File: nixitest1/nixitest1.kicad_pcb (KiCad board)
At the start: 2 copper layers, 27 parts, among them Q1 60V 3A, Q10 HVN, Q11 HVN, Q12 HVN, Q13 HVN, Q2 HVN, Q3 HVN, Q4 HVN, Q5 HVN, Q6 HVN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

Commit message: Update design.
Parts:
- removed R5: 18kΩ 1206 1% 250mW, Resistor_SMD:R_1206_3216Metric
- added C2: 10uF 25V, Capacitor_SMD:C_0603_1608Metric, F.Cu at (94.2, 64.5)
- added C3: 100n, Capacitor_SMD:C_0402_1005Metric, F.Cu at (83.5, 69.8)
- added J1: MSYS, Connector_PinHeader_2.54mm:PinHeader_2x05_P2.54mm_Horizontal, F.Cu at (84.9, 61.6)
- added J2: ~, rawpad22:rawpad22, F.Cu at (83.0, 95.0)
- added J3: ~, rawpad22:rawpad22, F.Cu at (90.0, 95.0)
- added J4: ~, rawpad22:rawpad22, F.Cu at (97.0, 95.0)
- moved NE2 49.5 mm to (80.2, 73.5), turned to -90 degrees
- moved R6 39.9 mm to (82.5, 89.1), turned to -150 degrees
- moved C1 34.8 mm to (97.9, 67.0), turned to 180 degrees
- moved R3 33.8 mm to (85.3, 64.1)
- moved NE1 33.8 mm to (80.2, 86.3), turned to -90 degrees
- moved Q9 33.5 mm to (93.0, 77.0), turned to 90 degrees
- moved R7 32.4 mm to (81.5, 82.5), turned to 180 degrees
- moved Q2 29.4 mm to (86.0, 77.7), turned to 180 degrees
- moved T1 22.9 mm to (94.0, 67.4), turned to -90 degrees
- moved Q1 21.9 mm to (90.4, 67.5)
- moved Q13 19.4 mm to (81.4, 79.0), turned to -90 degrees
- moved R1 18.9 mm to (90.2, 64.7)
- moved R2 17.7 mm to (92.0, 74.0)
- moved Q5 17.1 mm to (98.1, 82.0), turned to 180 degrees
- moved R4 9.02 mm to (98.0, 72.4), turned to 180 degrees
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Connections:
- NE1 pad 1: Net-(NE1-Pad1) -> ANODE
- NE2 pad 1: Net-(NE1-Pad1) -> ANODE
- U1 pad 15: unconnected-(U1-Pad15) -> PGM
- U1 pad 19: unconnected-(U1-Pad19) -> URX
- U1 pad 20: unconnected-(U1-Pad20) -> UTX
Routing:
- net GND: track 0.00 -> 140.2 mm, vias 0 -> 60
- net ANODE: track 0.00 -> 33.2 mm, vias 0 -> 2
- net +5V: track 0.00 -> 31.3 mm, vias 0 -> 1
- net DIG_5: track 0.00 -> 29.3 mm, vias 0 -> 2
- net DIG_4: track 0.00 -> 26.9 mm, vias 0 -> 2
- net DIG_3: track 0.00 -> 26.2 mm, vias 0 -> 2
- net DIG_8: track 0.00 -> 24.3 mm, vias 0 -> 2
- net DIG_7: track 0.00 -> 23.4 mm, vias 0 -> 2
- net DIG_2: track 0.00 -> 22.9 mm, vias 0 -> 2
- net DIG_6: track 0.00 -> 21.8 mm, vias 0 -> 2
- net DIG_9: track 0.00 -> 19.4 mm, vias 0 -> 2
- net DIG_1: track 0.00 -> 18.5 mm, vias 0 -> 2
- net Net-(C1-Pad1): track 0.00 -> 18.3 mm
- net HVVMON: track 0.00 -> 15.6 mm, vias 0 -> 2
- net DIG_0: track 0.00 -> 14.6 mm, vias 0 -> 2
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- added copper zone on B.Cu, net GND
- added copper zone on F.Cu, net GND
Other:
- board outline added: 22 x 38 mm
- board text added: "*"
- board text added: "nixitest1 rev-"

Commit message: Ok actually ready for production.
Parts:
- R1: value 300mΩ -> 500mΩ; footprint Resistor_SMD:R_1206_3216Metric -> Resistor_SMD:R_0805_2012Metric
- moved C2 0.55 mm to (94.0, 64.9)
- moved J1 0.37 mm to (84.9, 62.0)
- moved T1 0.26 mm to (94.0, 67.7)
- moved R1 0.23 mm to (90.3, 64.9)
- moved R3 0.23 mm to (85.3, 64.3)
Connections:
- J3 pad 1: GND -> +5V
- J4 pad 1: GND -> PGM
- U1 pad 1: HVCTL -> DIG_AUX
- U1 pad 2: DIG_AUX -> HVCTL
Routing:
- net +5V: track 31.3 -> 78.6 mm, vias 1 -> 2
- net PGM: track 11.1 -> 55.9 mm, vias 0 -> 1
- net GND: track 140.2 -> 172.8 mm, vias 60 -> 65
- net DIG_AUX: track 13.3 -> 14.1 mm
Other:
- board text added: "GND"
- board text added: "PGM"
- board text added: "VCC"

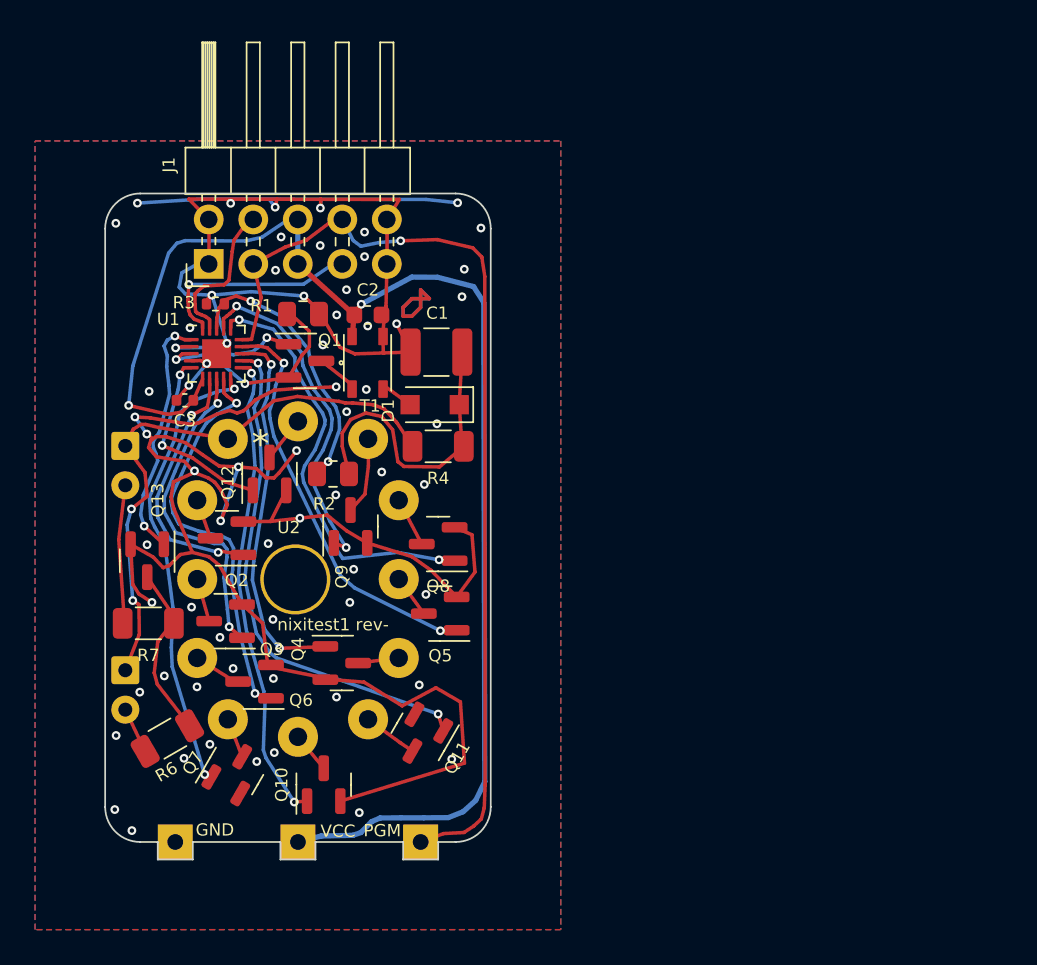
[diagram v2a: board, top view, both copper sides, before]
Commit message: Update design based on tests of first rev.
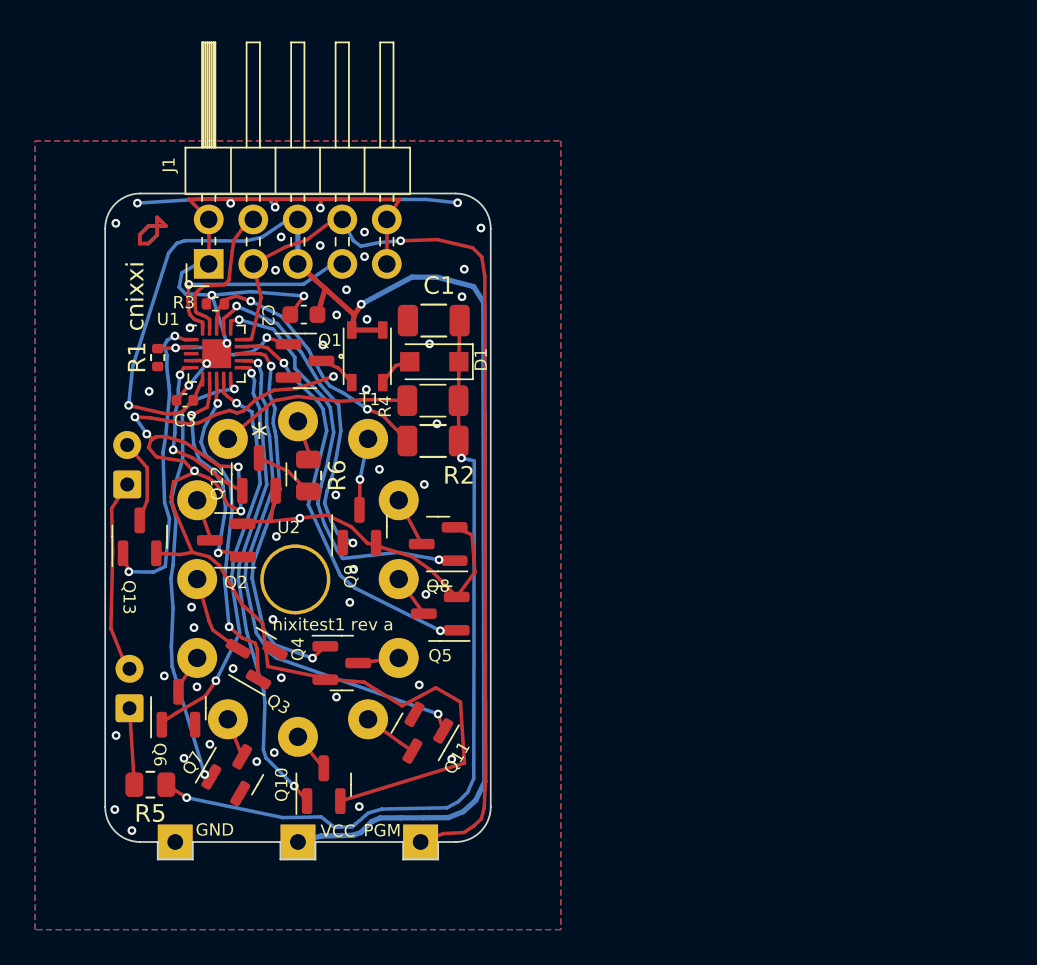
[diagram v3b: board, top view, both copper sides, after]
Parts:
- removed R7: 18kΩ 1206 1% 250mW, Resistor_SMD:R_1206_3216Metric
- added R5: 68kΩ 125mW, Resistor_SMD:R_0805_2012Metric, F.Cu at (81.6, 91.7)
- C1: footprint Capacitor_SMD:C_1210_3225Metric -> Capacitor_SMD:C_1206_3216Metric
- R1: value 500mΩ -> 10k; footprint Resistor_SMD:R_0805_2012Metric -> Resistor_SMD:R_0402_1005Metric
- R2: footprint Resistor_SMD:R_0805_2012Metric -> Resistor_SMD:R_1206_3216Metric
- R4: value 18kΩ 1206 1% 250mW -> 15kΩ 1206 1% 250mW
- R6: value 18kΩ 1206 1% 250mW -> 68kΩ 125mW; footprint Resistor_SMD:R_1206_3216Metric -> Resistor_SMD:R_0805_2012Metric
- moved R6 17.0 mm to (90.6, 74.1), turned to -90 degrees
- moved R1 8.65 mm to (82.0, 67.4), turned to 90 degrees
- moved R2 6.01 mm to (97.7, 72.1)
- moved Q6 4.60 mm to (83.2, 87.4), turned to 90 degrees
- moved C2 3.65 mm to (90.3, 64.9), turned to 180 degrees
- moved R4 2.62 mm to (97.7, 69.8)
- moved Q3 2.56 mm to (87.4, 84.4), turned to 150 degrees
- moved D1 2.45 mm to (97.8, 67.6)
- moved C1 1.81 mm to (97.8, 65.2)
- moved Q13 1.43 mm to (81.0, 77.6), turned to 90 degrees
- moved Q12 0.60 mm to (87.8, 74.0)
- moved Q9 0.51 mm to (93.5, 77.0)
- moved T1 0.37 mm to (94.0, 67.3)
- moved NE1 0.24 mm to (80.4, 86.3), turned to 90 degrees
- moved Q2 0.13 mm to (85.9, 77.8)
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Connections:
- net Net-(C1-Pad1) renamed HV
- NE1 pad 1: ANODE -> Net-(NE1-Pad1)
- NE1 pad 2: Net-(NE1-Pad2) -> Net-(NE2-Pad1)
- NE2 pad 1: ANODE -> Net-(NE2-Pad1)
- NE2 pad 2: Net-(NE2-Pad2) -> CATHAUX
- Q1 pad 2: HVIMON -> GND
- Q12 pad 3: CATHDOT -> Net-(Q12-Pad3)
- R1 pad 1: HVIMON -> GND
- R1 pad 2: GND -> HVCTL
- R6 pad 1: CATHAUX -> CATHDOT
- R6 pad 2: Net-(NE1-Pad2) -> Net-(Q12-Pad3)
- T1 pad 2: GND -> +5V
- U1 pad 3: HVIMON -> unconnected-(U1-Pad3)
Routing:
- net HV: track 18.3 -> 45.0 mm, vias 0 -> 2
- net GND: track 172.8 -> 147.7 mm, vias 65 -> 60
- net ANODE: track 33.1 -> 11.1 mm, vias 2 -> 0
- net HVIMON: track 12.9 -> 0.00 mm, vias 2 -> 0
- net Net-(NE2-Pad1): track 0.00 -> 11.0 mm
- net Net-(NE2-Pad2): track 7.63 -> 0.00 mm
- net CATHAUX: track 9.99 -> 4.81 mm
- net Net-(NE1-Pad1): track 0.00 -> 4.37 mm
- net DIG_AUX: track 14.1 -> 17.8 mm
- net Net-(Q12-Pad3): track 0.00 -> 3.45 mm
- net +5V: track 78.6 -> 81.6 mm
- net Net-(NE1-Pad2): track 2.64 -> 0.00 mm
- net CATH1: track 2.50 -> 4.85 mm
- net DIG_0: track 14.6 -> 12.6 mm
- net DIG_DOT: track 10.9 -> 9.81 mm
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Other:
- board text added: "cnixxi"
- board text added: "nixitest1 rev a"
- board text removed: "nixitest1 rev-"

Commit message: Update schematic and design.
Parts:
- added J5: ~, rawpad22:rawpad22, F.Cu at (94.0, 95.0)
- added J6: ~, rawpad22:rawpad22, F.Cu at (98.0, 95.0)
- moved J4 11.0 mm to (86.0, 95.0)
- moved J2 1.00 mm to (82.0, 95.0)
- moved NE2 0.22 mm to (80.4, 73.6)
- moved R4 0.09 mm to (97.7, 69.9)
- moved R2 0.06 mm to (97.7, 72.2)
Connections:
- J4 pad 1: PGM -> URX
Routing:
- net UTX: track 12.2 -> 52.8 mm, vias 1 -> 3
- net URX: track 8.86 -> 46.2 mm, vias 0 -> 1
- net GND: track 147.7 -> 131.3 mm, vias 60 -> 76
- net HV: track 45.0 -> 41.4 mm
- net PGM: track 55.9 -> 56.9 mm
- net +5V: track 81.6 -> 82.1 mm
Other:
- board size 22 x 38 mm -> 22 x 37.9 mm
- board text added: "URX"
- board text added: "UTX"

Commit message: Updte with schematic.
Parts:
- moved J2 0.38 mm to (82.0, 95.4)
- moved J3 0.38 mm to (90.0, 95.4)
- moved J4 0.38 mm to (86.0, 95.4)
- moved J5 0.38 mm to (94.0, 95.4)
- moved J6 0.38 mm to (98.0, 95.4)
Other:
- board size 22 x 37.9 mm -> 22 x 38.2 mm
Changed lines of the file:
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@@
     )
     (pad_to_mask_clearance 0)
+    (grid_origin 79 93)
     (pcbplotparams
       (layerselection 0x00010fc_ffffffff)
@@
       (drillshape 0)
       (scaleselection 1)
-      (outputdirectory "nixitest1-rev-")
+      (outputdirectory "nixitest1-revA")
     )
   )
@@
   (net 39 "unconnected-(U1-Pad3)")
   (footprint "rawpad22:rawpad22" (layer "F.Cu")
-    (at 98 95)
+    (at 98 95.375)
     (property "Sheetfile" "nixitest1.kicad_sch")
     (property "Sheetname" "")
@@
     (fp_line (start -1.6 0.8) (end -1.6 -0.8) (layer "F.Fab") (width 0.1))
     (fp_line (start -1.6 -0.8) (end 1.6 -0.8) (layer "F.Fab") (width 0.1))
-    (pad "1" smd roundrect (at -1.475 0 180) (size 1.15 1.8) (layers "F.Cu" "F.Paste" "F.Mask") (roundrect_rratio 0.217391)
+    (pad "1" smd roundrect (at -1.475 0 180) (size 1.15 1.8) (layers "F.Cu" "F.Paste" "F.Mask") (roundrect_rratio 0.2173913043)
       (net 31 "HV") (pintype "passive"))
-    (pad "2" smd roundrect (at 1.475 0 180) (size 1.15 1.8) (layers "F.Cu" "F.Paste" "F.Mask") (roundrect_rratio 0.217391)
+    (pad "2" smd roundrect (at 1.475 0 180) (size 1.15 1.8) (layers "F.Cu" "F.Paste" "F.Mask") (roundrect_rratio 0.2173913043)
       (net 1 "GND") (pintype "passive"))
     (model "${KICAD6_3DMODEL_DIR}/Capacitor_SMD.3dshapes/C_1206_3216Metric.wrl"
@@
   )
   (footprint "rawpad22:rawpad22" (layer "F.Cu")
-    (at 94 95)
+    (at 94 95.375)
     (property "Sheetfile" "nixitest1.kicad_sch")
     (property "Sheetname" "")
@@
     (fp_line (start -1 0.625) (end -1 -0.625) (layer "F.Fab") (width 0.1))
     (fp_line (start 1 -0.625) (end 1 0.625) (layer "F.Fab") (width 0.1))
-    (pad "1" smd roundrect (at -0.9125 0 270) (size 1.025 1.4) (layers "F.Cu" "F.Paste" "F.Mask") (roundrect_rratio 0.243902)
+    (pad "1" smd roundrect (at -0.9125 0 270) (size 1.025 1.4) (layers "F.Cu" "F.Paste" "F.Mask") (roundrect_rratio 0.243902439)
       (net 26 "CATHDOT") (pintype "passive"))
-    (pad "2" smd roundrect (at 0.9125 0 270) (size 1.025 1.4) (layers "F.Cu" "F.Paste" "F.Mask") (roundrect_rratio 0.243902)
+    (pad "2" smd roundrect (at 0.9125 0 270) (size 1.025 1.4) (layers "F.Cu" "F.Paste" "F.Mask") (roundrect_rratio 0.243902439)
       (net 38 "Net-(Q12-Pad3)") (pintype "passive"))
     (model "${KICAD6_3DMODEL_DIR}/Resistor_SMD.3dshapes/R_0805_2012Metric.wrl"
@@
   )
   (footprint "rawpad22:rawpad22" (layer "F.Cu")
-    (at 90 95)
+    (at 90 95.375)
     (property "Sheetfile" "nixitest1.kicad_sch")
     (property "Sheetname" "")
@@
     (fp_line (start 1.6 0.8) (end -1.6 0.8) (layer "F.Fab") (width 0.1))
     (fp_line (start 1.6 -0.8) (end 1.6 0.8) (layer "F.Fab") (width 0.1))
-    (pad "1" smd roundrect (at -1.4625 0) (size 1.125 1.75) (layers "F.Cu" "F.Paste" "F.Mask") (roundrect_rratio 0.222222)
+    (pad "1" smd roundrect (at -1.4625 0) (size 1.125 1.75) (layers "F.Cu" "F.Paste" "F.Mask") (roundrect_rratio 0.2222222222)
       (net 29 "HVVMON") (pintype "passive"))
-    (pad "2" smd roundrect (at 1.4625 0) (size 1.125 1.75) (layers "F.Cu" "F.Paste" "F.Mask") (roundrect_rratio 0.222222)
+    (pad "2" smd roundrect (at 1.4625 0) (size 1.125 1.75) (layers "F.Cu" "F.Paste" "F.Mask") (roundrect_rratio 0.2222222222)
       (net 31 "HV") (pintype "passive"))
     (model "${KICAD6_3DMODEL_DIR}/Resistor_SMD.3dshapes/R_1206_3216Metric.wrl"
@@
   )
   (footprint "rawpad22:rawpad22" (layer "F.Cu")
-    (at 86 95)
+    (at 86 95.375)
     (property "Sheetfile" "nixitest1.kicad_sch")
     (property "Sheetname" "")
@@
   )
   (footprint "rawpad22:rawpad22" (layer "F.Cu")
-    (at 82 95)
+    (at 82 95.375)
     (property "Sheetfile" "nixitest1.kicad_sch")
     (property "Sheetname" "")
@@
     (fp_line (start 1 0.625) (end -1 0.625) (layer "F.Fab") (width 0.1))
     (fp_line (start 1 -0.625) (end 1 0.625) (layer "F.Fab") (width 0.1))
-    (pad "1" smd roundrect (at -0.9125 0 180) (size 1.025 1.4) (layers "F.Cu" "F.Paste" "F.Mask") (roundrect_rratio 0.243902)
+    (pad "1" smd roundrect (at -0.9125 0 180) (size 1.025 1.4) (layers "F.Cu" "F.Paste" "F.Mask") (roundrect_rratio 0.243902439)
       (net 31 "HV") (pintype "passive"))
-    (pad "2" smd roundrect (at 0.9125 0 180) (size 1.025 1.4) (layers "F.Cu" "F.Paste" "F.Mask") (roundrect_rratio 0.243902)
+    (pad "2" smd roundrect (at 0.9125 0 180) (size 1.025 1.4) (layers "F.Cu" "F.Paste" "F.Mask") (roundrect_rratio 0.243902439)
       (net 32 "Net-(NE1-Pad1)") (pintype "passive"))
     (model "${KICAD6_3DMODEL_DIR}/Resistor_SMD.3dshapes/R_0805_2012Metric.wrl"
@@
   (gr_line (start 80.97 60.86) (end 80.97 60.36) (layer "F.Mask") (width 0.15))
   (gr_line (start 79 60) (end 79 93) (layer "Edge.Cuts") (width 0.1))
-  (gr_line (start 93.125 95.875) (end 93.125 95) (layer "Edge.Cuts") (width 0.1))
-  (gr_line (start 94.875 95.875) (end 93.125 95.875) (layer "Edge.Cuts") (width 0.1))
+  (gr_line (start 93.125 96.25) (end 93.125 95) (layer "Edge.Cuts") (width 0.1))
+  (gr_line (start 94.875 96.25) (end 93.125 96.25) (layer "Edge.Cuts") (width 0.1))
   (gr_arc (start 101 93) (mid 100.414214 94.414214) (end 99 95) (layer "Edge.Cuts") (width 0.1))
-  (gr_line (start 90.875 95.875) (end 89.125 95.875) (layer "Edge.Cuts") (width 0.1))
-  (gr_line (start 86.875 95) (end 86.875 95.875) (layer "Edge.Cuts") (width 0.1))
-  (gr_line (start 81.125 95.875) (end 82.875 95.875) (layer "Edge.Cuts") (width 0.1))
+  (gr_line (start 90.875 96.25) (end 89.125 96.25) (layer "Edge.Cuts") (width 0.1))
+  (gr_line (start 86.875 95) (end 86.875 96.25) (layer "Edge.Cuts") (width 0.1))
+  (gr_line (start 81.125 96.25) (end 82.875 96.25) (layer "Edge.Cuts") (width 0.1))
   (gr_line (start 90.875 95) (end 93.125 95) (layer "Edge.Cuts") (width 0.1))
   (gr_line (start 101 93) (end 101 60) (layer "Edge.Cuts") (width 0.1))
   (gr_arc (start 81 95) (mid 79.585786 94.414214) (end 79 93) (layer "Edge.Cuts") (width 0.1))
   (gr_line (start 82.875 95) (end 85.125 95) (layer "Edge.Cuts") (width 0.1))
-  (gr_line (start 98.875 95.875) (end 97.125 95.875) (layer "Edge.Cuts") (width 0.1))
-  (gr_line (start 82.875 95.875) (end 82.875 95) (layer "Edge.Cuts") (width 0.1))
+  (gr_line (start 98.875 96.25) (end 97.125 96.25) (layer "Edge.Cuts") (width 0.1))
+  (gr_line (start 82.875 96.25) (end 82.875 95) (layer "Edge.Cuts") (width 0.1))
   (gr_line (start 99 95) (end 98.875 95) (layer "Edge.Cuts") (width 0.1))
   (gr_line (start 81 58) (end 99 58) (layer "Edge.Cuts") (width 0.1))
   (gr_line (start 81 95) (end 81.125 95) (layer "Edge.Cuts") (width 0.1))
-  (gr_line (start 89.125 95.875) (end 89.125 95) (layer "Edge.Cuts") (width 0.1))
-  (gr_line (start 94.875 95) (end 94.875 95.875) (layer "Edge.Cuts") (width 0.1))
-  (gr_line (start 85.125 95.875) (end 85.125 95) (layer "Edge.Cuts") (width 0.1))
-  (gr_line (start 90.875 95) (end 90.875 95.875) (layer "Edge.Cuts") (width 0.1))
+  (gr_line (start 89.125 96.25) (end 89.125 95) (layer "Edge.Cuts") (width 0.1))
+  (gr_line (start 94.875 95) (end 94.875 96.25) (layer "Edge.Cuts") (width 0.1))
+  (gr_line (start 85.125 96.25) (end 85.125 95) (layer "Edge.Cuts") (width 0.1))
+  (gr_line (start 90.875 95) (end 90.875 96.25) (layer "Edge.Cuts") (width 0.1))
   (gr_arc (start 79 60) (mid 79.585786 58.585786) (end 81 58) (layer "Edge.Cuts") (width 0.1))
   (gr_line (start 86.875 95) (end 89.125 95) (layer "Edge.Cuts") (width 0.1))
-  (gr_line (start 81.125 95) (end 81.125 95.875) (layer "Edge.Cuts") (width 0.1))
+  (gr_line (start 81.125 95) (end 81.125 96.25) (layer "Edge.Cuts") (width 0.1))
   (gr_arc (start 99 58) (mid 100.414214 58.585786) (end 101 60) (layer "Edge.Cuts") (width 0.1))
-  (gr_line (start 98.875 95) (end 98.875 95.875) (layer "Edge.Cuts") (width 0.1))
-  (gr_line (start 86.875 95.875) (end 85.125 95.875) (layer "Edge.Cuts") (width 0.1))
-  (gr_line (start 97.125 95.875) (end 97.125 95) (layer "Edge.Cuts") (width 0.1))
+  (gr_line (start 98.875 95) (end 98.875 96.25) (layer "Edge.Cuts") (width 0.1))
+  (gr_line (start 86.875 96.25) (end 85.125 96.25) (layer "Edge.Cuts") (width 0.1))
+  (gr_line (start 97.125 96.25) (end 97.125 95) (layer "Edge.Cuts") (width 0.1))
   (gr_line (start 94.875 95) (end 97.125 95) (layer "Edge.Cuts") (width 0.1))
   (gr_text "*" (at 87.42 71.84 -120) (layer "B.SilkS")

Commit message: Tweak pins.
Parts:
- moved J2 0.25 mm to (82.0, 95.1)
- moved J3 0.25 mm to (90.0, 95.1)
- moved J4 0.25 mm to (86.0, 95.1)
- moved J5 0.25 mm to (94.0, 95.1)
- moved J6 0.25 mm to (98.0, 95.1)
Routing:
- net GND: vias 76 -> 79
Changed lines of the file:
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@@
   (net 39 "unconnected-(U1-Pad3)")
   (footprint "rawpad22:rawpad22" (layer "F.Cu")
-    (at 98 95.375)
+    (at 98 95.125)
     (property "Sheetfile" "nixitest1.kicad_sch")
     (property "Sheetname" "")
@@
       (effects (font (size 1 1) (thickness 0.15)))
     )
-    (pad "1" thru_hole rect (at 0 0) (size 1.75 1.75) (drill 0.9) (layers *.Cu *.Mask)
+    (pad "1" thru_hole rect (at 0 0) (size 1.75 2.25) (drill 0.9) (layers *.Cu *.Mask)
       (net 36 "UTX") (pinfunction "Pin_1") (pintype "passive"))
   )
@@
   )
   (footprint "rawpad22:rawpad22" (layer "F.Cu")
-    (at 94 95.375)
+    (at 94 95.125)
     (property "Sheetfile" "nixitest1.kicad_sch")
     (property "Sheetname" "")
@@
       (effects (font (size 1 1) (thickness 0.15)))
     )
-    (pad "1" thru_hole rect (at 0 0) (size 1.75 1.75) (drill 0.9) (layers *.Cu *.Mask)
+    (pad "1" thru_hole rect (at 0 0) (size 1.75 2.25) (drill 0.9) (layers *.Cu *.Mask)
       (net 34 "PGM") (pinfunction "Pin_1") (pintype "passive"))
   )
@@
   )
   (footprint "rawpad22:rawpad22" (layer "F.Cu")
-    (at 90 95.375)
+    (at 90 95.125)
     (property "Sheetfile" "nixitest1.kicad_sch")
     (property "Sheetname" "")
@@
       (effects (font (size 1 1) (thickness 0.15)))
     )
-    (pad "1" thru_hole rect (at 0 0) (size 1.75 1.75) (drill 0.9) (layers *.Cu *.Mask)
+    (pad "1" thru_hole rect (at 0 0) (size 1.75 2.25) (drill 0.9) (layers *.Cu *.Mask)
       (net 33 "+5V") (pinfunction "Pin_1") (pintype "passive"))
   )
@@
   )
   (footprint "rawpad22:rawpad22" (layer "F.Cu")
-    (at 86 95.375)
+    (at 86 95.125)
     (property "Sheetfile" "nixitest1.kicad_sch")
     (property "Sheetname" "")
@@
       (effects (font (size 1 1) (thickness 0.15)))
     )
-    (pad "1" thru_hole rect (at 0 0) (size 1.75 1.75) (drill 0.9) (layers *.Cu *.Mask)
+    (pad "1" thru_hole rect (at 0 0) (size 1.75 2.25) (drill 0.9) (layers *.Cu *.Mask)
       (net 35 "URX") (pinfunction "Pin_1") (pintype "passive"))
   )
   (footprint "rawpad22:rawpad22" (layer "F.Cu")
-    (at 82 95.375)
+    (at 82 95.125)
     (property "Sheetfile" "nixitest1.kicad_sch")
     (property "Sheetname" "")
@@
       (effects (font (size 1 1) (thickness 0.15)))
     )
-    (pad "1" thru_hole rect (at 0 0) (size 1.75 1.75) (drill 0.9) (layers *.Cu *.Mask)
+    (pad "1" thru_hole rect (at 0 0) (size 1.75 2.25) (drill 0.9) (layers *.Cu *.Mask)
       (net 1 "GND") (pinfunction "Pin_1") (pintype "passive"))
   )
@@
   (via (at 83.84 65.66) (size 0.5) (drill 0.25) (layers "F.Cu" "B.Cu") (free) (net 1))
   (via (at 84.07 82.77) (size 0.5) (drill 0.25) (layers "F.Cu" "B.Cu") (free) (net 1))
+  (via (at 94.625 90.125) (size 0.5) (drill 0.25) (layers "F.Cu" "B.Cu") (free) (net 1))
   (via (at 83.93 81.6) (size 0.5) (drill 0.25) (layers "F.Cu" "B.Cu") (free) (net 1))
   (via (at 87.65 90.41) (size 0.5) (drill 0.25) (layers "F.Cu" "B.Cu") (free) (net 1))
@@
   (via (at 93 92) (size 0.5) (drill 0.25) (layers "F.Cu" "B.Cu") (free) (net 1))
   (via (at 79.52 68.07) (size 0.5) (drill 0.25) (layers "F.Cu" "B.Cu") (free) (net 1))
+  (via (at 90.625 91.375) (size 0.5) (drill 0.25) (layers "F.Cu" "B.Cu") (free) (net 1))
+  (via (at 91.5 92.625) (size 0.5) (drill 0.25) (layers "F.Cu" "B.Cu") (free) (net 1))
   (via (at 99.48 83.83) (size 0.5) (drill 0.25) (layers "F.Cu" "B.Cu") (free) (net 1))
   (via (at 99.11 58.53) (size 0.5) (drill 0.25) (layers "F.Cu" "B.Cu") (free) (net 1))
